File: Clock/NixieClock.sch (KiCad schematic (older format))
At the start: 54 parts, among them J1 PJ-079BH, J2 Conn_02x10_Top_Bottom, J3 Conn_02x10_Top_Bottom, J4 Conn_02x10_Top_Bottom, J5 Conn_02x10_Odd_Even, J6 Conn_02x10_Odd_Even, J7 Conn_02x10_Odd_Even, Q1 2N2097, Q2 SI2333DDS-T1-GE3, Q3 T2N7002AK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

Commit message: Add v2.0 plots
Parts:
- removed C6: 10u, Capacitor_SMD:C_1210_3225Metric_Pad1.42x2.65mm_HandSolder, symbol Device:CP1_Small
- removed C7: 22u, Capacitor_SMD:C_1210_3225Metric_Pad1.42x2.65mm_HandSolder, symbol Device:CP1_Small
- removed C8: 4.7u, Capacitor_SMD:C_0603_1608Metric_Pad1.05x0.95mm_HandSolder, symbol Device:C_Small
- removed Q1: 2N2097, Package_TO_SOT_SMD:SOT-23_Handsoldering, symbol Transistor_BJT:2N3906
- removed Q4: 2N3906, Package_TO_SOT_SMD:SOT-23_Handsoldering, symbol Transistor_BJT:2N3906
- removed R5: 115k, Resistor_SMD:R_0603_1608Metric_Pad1.05x0.95mm_HandSolder, symbol Device:R_Small
- removed R6: 25.5k, Resistor_SMD:R_0603_1608Metric_Pad1.05x0.95mm_HandSolder, symbol Device:R_Small
- removed U5: AP65251, Package_TO_SOT_SMD:TSOT-23-6_HandSoldering, symbol Clock:AP65251
- added C6, C7: 22u, Capacitor_SMD:C_0805_2012Metric_Pad1.15x1.40mm_HandSolder, symbol Device:C_Small
- added D6: BZX84Cxx, Diode_SMD:D_SOT-23_ANK, symbol Diode:BZX84Cxx
- added Q1: 2N2907, Package_TO_SOT_SMD:SOT-23_Handsoldering, symbol Device:Q_PNP_BEC
- added Q4: 2N3906, Package_TO_SOT_SMD:SOT-23_Handsoldering, symbol Device:Q_PNP_BEC
- added Q5: SI2343DS, Package_TO_SOT_SMD:SOT-23_Handsoldering, symbol Clock:SI2333DDS-T1-GE3
- added U5: AP63203, Package_TO_SOT_SMD:TSOT-23-6, symbol Clock:AP63203
- C1: value 220u -> 330u
- C5: value 33p -> 10u; footprint Capacitor_SMD:C_0603_1608Metric_Pad1.05x0.95mm_HandSolder -> Capacitor_SMD:C_0805_2012Metric_Pad1.15x1.40mm_HandSolder
- Q2: value SI2333DDS-T1-GE3 -> SI2343DS
- R10, R11, R8, R9: value 22k -> 33.2k
- R12: value 20 -> 22
- R14: value 115k -> 499k
- R7: value 680 -> 2k
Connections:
- net +12V: now also C5.1, J2.6 (Pin_6), J5.15 (Pin_15), U5.2 (EN), U5.3 (VIN)
- net +12V_UNSAFE: now also Q4.1 (B)
- net +170V: now also J2.2 (Pin_2), J5.19 (Pin_19)
- net +3.3V: now also C6.1, C7.1, D6.1 (K), U5.1 (FB); no longer C5.1
- net GND: now also C5.2, C6.2, C7.2, D6.2 (A), Q1.3 (C), Q4.3 (C), U5.4 (GND)
- net at C1.1, R1.1, U1.1 (SwC)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: now also Q5.2 (S); no longer L1.1
- net at D2.2 (A), R4.2, U1.2 (SwE): now also Q1.1 (B)
- net at D2.1 (K), U4.1 (G): now also Q1.2 (E)
- net at C4.1: now also U5.6 (BST)
- net at C4.2, L2.1: now also U5.5 (SW)
- net T_ON: now reaches Q2.1 (G), Q3.3 (D), R13.2
- net T_ON: now also Q5.1 (G)
- net at C9.1, Q3.1 (G), R14.1: now also Q4.2 (E)
- new net: L1.1, Q5.3 (D)
- no-connect marks 46 -> 42
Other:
- moved on the sheet: C1, C4, L2

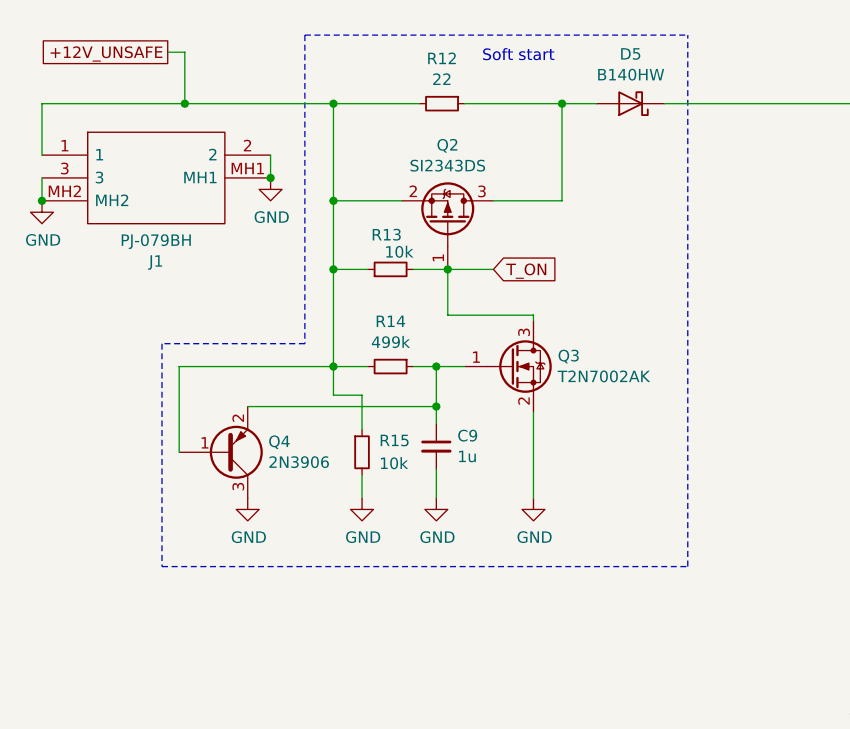
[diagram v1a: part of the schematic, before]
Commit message: Remove a "fast-discharge" transistor, as it was not operating as intended due to emitter-base breakdown. It was pretty much optional anyway.
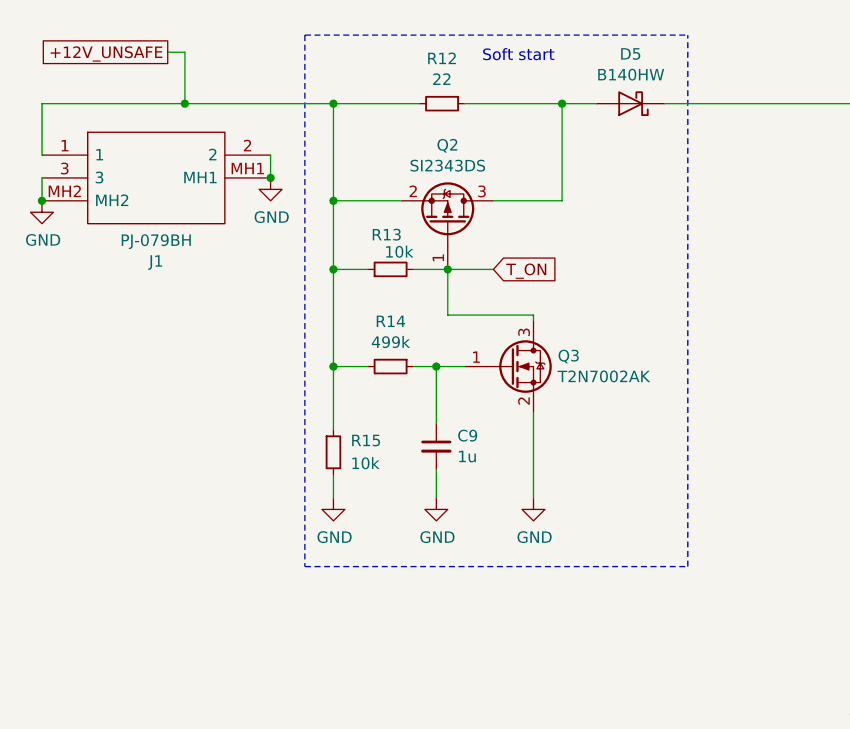
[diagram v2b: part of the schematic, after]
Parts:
- removed Q4: 2N3906, Package_TO_SOT_SMD:SOT-23_Handsoldering, symbol Device:Q_PNP_BEC
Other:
- moved on the sheet: R15
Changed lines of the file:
@@
 EESchema Schematic File Version 4
-LIBS:NixieClock-cache
 EELAYER 30 0
 EELAYER END
@@
 Wire Wire Line
 	-650 825  -1075 825
-$Comp
-L power:GND #PWR0101
-U 1 1 5D698A9B
-P -2025 2550
-F 0 "#PWR0101" H -2025 2300 50  0001 C CNN
-F 1 "GND" H -2020 2377 50  0000 C CNN
-F 2 "" H -2025 2550 50  0001 C CNN
-F 3 "" H -2025 2550 50  0001 C CNN
-	1    -2025 2550
-	1    0    0    -1
-$EndComp
 Wire Wire Line
 	-1650 1550 -1650 1250
@@
 Wire Wire Line
 	-1500 1975 -1650 1975
-Wire Wire Line
-	-1200 2225 -1200 2150
 Connection ~ -1200 1975
 Wire Wire Line
 	-1200 1975 -1075 1975
-Wire Wire Line
-	-2325 2350 -2325 1975
 Connection ~ -1650 1975
-Wire Wire Line
-	-2325 1975 -1650 1975
-Wire Wire Line
-	-2025 2150 -1200 2150
-Connection ~ -1200 2150
-Wire Wire Line
-	-1200 2150 -1200 1975
 $Comp
 L power:GND #PWR0102
@@
 	-775 2175 -775 2550
 Wire Notes Line
-	-1775 1875 -2400 1875
-Wire Notes Line
-	-2400 1875 -2400 2850
-Wire Notes Line
 	-100 2850 -100 525
-Wire Notes Line
-	-1775 525  -1775 1875
 Text Notes -1000 650  0    50   ~ 0
 Soft start
@@
 Wire Notes Line
 	-1775 525  -100 525
-Wire Notes Line
-	-2400 2850 -100 2850
 $Comp
 L Device:Fuse F1
@@
 L Device:R_Small R15
 U 1 1 5D83C7C9
-P -1525 2350
-F 0 "R15" H -1450 2400 50  0000 L CNN
-F 1 "10k" H -1450 2300 50  0000 L CNN
-F 2 "Resistor_SMD:R_0603_1608Metric_Pad1.05x0.95mm_HandSolder" H -1525 2350 50  0001 C CNN
-F 3 "~" H -1525 2350 50  0001 C CNN
-	1    -1525 2350
-	1    0    0    -1
-$EndComp
-Wire Wire Line
-	-1650 1975 -1650 2100
-Wire Wire Line
-	-1650 2100 -1525 2100
-Wire Wire Line
-	-1525 2100 -1525 2250
-$Comp
-L power:GND #PWR0104
-U 1 1 5D8454C0
-P -1525 2550
-F 0 "#PWR0104" H -1525 2300 50  0001 C CNN
-F 1 "GND" H -1520 2377 50  0000 C CNN
-F 2 "" H -1525 2550 50  0001 C CNN
-F 3 "" H -1525 2550 50  0001 C CNN
-	1    -1525 2550
-	1    0    0    -1
-$EndComp
-Wire Wire Line
-	-1525 2450 -1525 2550
+P -1650 2350
+F 0 "R15" H -1575 2400 50  0000 L CNN
+F 1 "10k" H -1575 2300 50  0000 L CNN
+F 2 "Resistor_SMD:R_0603_1608Metric_Pad1.05x0.95mm_HandSolder" H -1650 2350 50  0001 C CNN
+F 3 "~" H -1650 2350 50  0001 C CNN
+	1    -1650 2350
+	1    0    0    -1
+$EndComp
 Wire Wire Line
 	3900 1975 3900 2575
@@
 +12V
 $Comp
-L Device:Q_PNP_BEC Q4
-U 1 1 5D935C20
-P -2125 2350
-F 0 "Q4" H -1935 2304 50  0000 L CNN
-F 1 "2N3906" H -1935 2395 50  0000 L CNN
-F 2 "Package_TO_SOT_SMD:SOT-23_Handsoldering" H -1925 2450 50  0001 C CNN
-F 3 "~" H -2125 2350 50  0001 C CNN
-	1    -2125 2350
-	1    0    0    1
-$EndComp
-$Comp
 L Diode:BZX84Cxx D6
 U 1 1 5D984DE8
@@
 Text GLabel 3550 1125 3    50   Input ~ 0
 T_ON
+Wire Wire Line
+	-1200 1975 -1200 2225
+$Comp
+L power:GND #PWR?
+U 1 1 5E0ED859
+P -1650 2550
+F 0 "#PWR?" H -1650 2300 50  0001 C CNN
+F 1 "GND" H -1645 2377 50  0000 C CNN
+F 2 "" H -1650 2550 50  0001 C CNN
+F 3 "" H -1650 2550 50  0001 C CNN
+	1    -1650 2550
+	1    0    0    -1
+$EndComp
+Wire Wire Line
+	-1650 1975 -1650 2250
+Wire Wire Line
+	-1650 2550 -1650 2450
+Wire Notes Line
+	-1775 2850 -100 2850
+Wire Notes Line
+	-1775 525  -1775 2850
 $EndSCHEMATC
